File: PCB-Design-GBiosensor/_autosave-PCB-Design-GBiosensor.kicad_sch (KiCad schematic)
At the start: 15 parts, among them J1 Conn_01x03_Pin, U1 TLV172IDCK, U2 TLV172IDCK

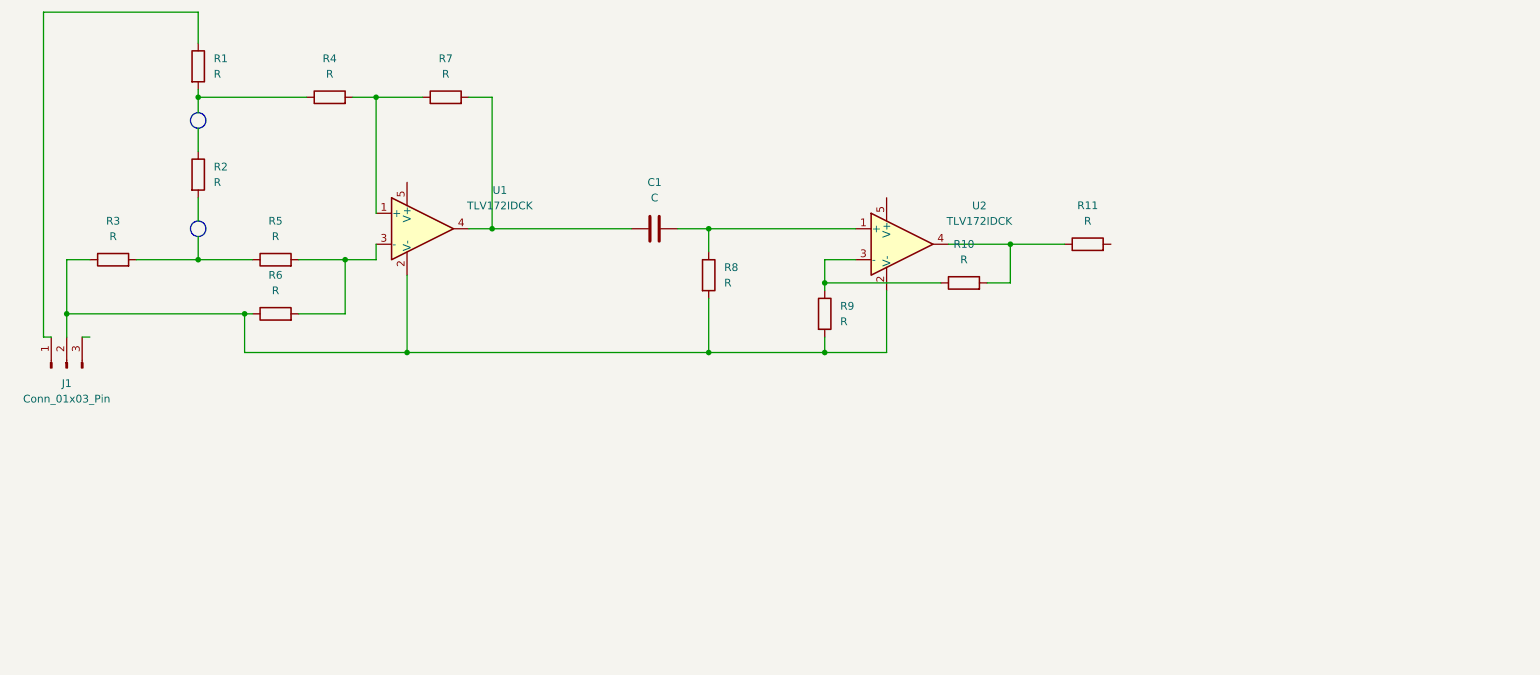
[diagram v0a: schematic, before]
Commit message: just changed connector and added a power flag
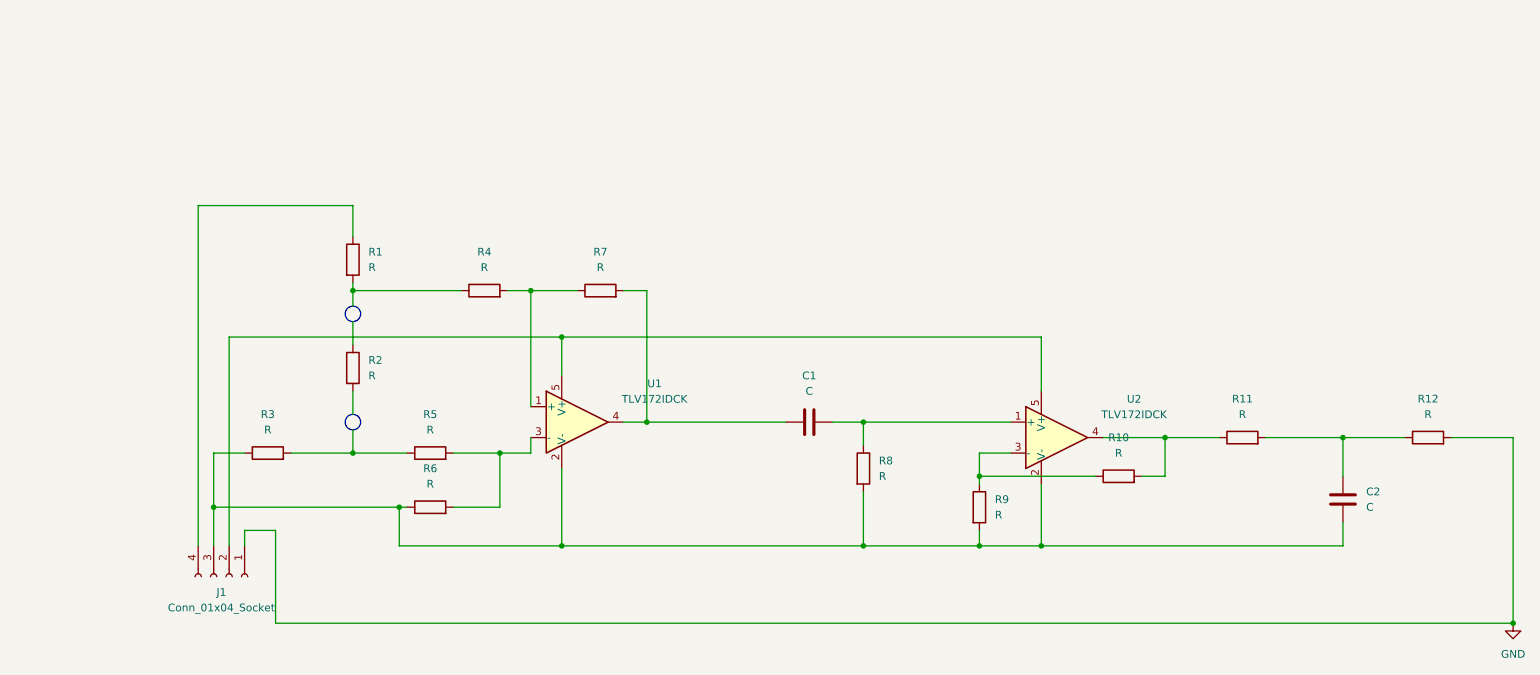
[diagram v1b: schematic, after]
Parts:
- removed J1: Conn_01x03_Pin, symbol Connector:Conn_01x03_Pin
- added C2: C, symbol Device:C
- added J1: Conn_01x04_Socket, symbol Connector:Conn_01x04_Socket
- added R12: R, symbol Device:R
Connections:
- net at R3.1, R6.1, R8.2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: now also C2.2, J1.3 (Pin_3)
- net at U2.5 (V+): now also U1.5 (V+), J1.2 (Pin_2)
- net at R1.1: now also J1.4 (Pin_4)
- net at R11.2: now also C2.1, R12.1
- new net GND: J1.1 (Pin_1), R12.2
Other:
- moved on the sheet: C1, R1, R10, R11, R2, R3, R4, R5, R6, R7, R8, R9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
